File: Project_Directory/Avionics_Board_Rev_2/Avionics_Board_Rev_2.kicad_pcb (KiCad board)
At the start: 2 copper layers, 22 x 16 mm, 22 parts, among them J1 Battery, J10 PWM_1, J11 PWM_2, J12 PWM_3, J13 I2C, J14 UART, J2 ARM, J3 PYRO_1, J7 PWM_4, J8 PWM_5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

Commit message: more work
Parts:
- added C10: IRFR024NPBF, VelR:IRFR024NTRPBF-HXY Mosfet, F.Cu at (159.2, 154.5)
- added C7: IRFR024NPBF, VelR:IRFR024NTRPBF-HXY Mosfet, F.Cu at (161.5, 137.0)
- added C8: IRFR024NPBF, VelR:IRFR024NTRPBF-HXY Mosfet, F.Cu at (179.2, 168.9)
- added C9: IRFR024NPBF, VelR:IRFR024NTRPBF-HXY Mosfet, F.Cu at (179.2, 154.9)
- added D3: B120-E3, Diode_SMD:D_SMA, F.Cu at (186.6, 169.6)
- added D4: B120-E3, Diode_SMD:D_SMA, F.Cu at (187.0, 156.0)
- added D5: B120-E3, Diode_SMD:D_SMA, B.Cu at (153.8, 154.8)
- added J4: PYRO_1, TerminalBlock_Phoenix:TerminalBlock_Phoenix_MKDS-1,5-2_1x02_P5.00mm_Horizontal, F.Cu at (193.8, 171.3)
- added J5: PYRO_1, TerminalBlock_Phoenix:TerminalBlock_Phoenix_MKDS-1,5-2_1x02_P5.00mm_Horizontal, F.Cu at (193.8, 157.7)
- added J6: PYRO_1, TerminalBlock_Phoenix:TerminalBlock_Phoenix_MKDS-1,5-2_1x02_P5.00mm_Horizontal, F.Cu at (146.0, 152.3)
- added U2: LoRa, VelR:RFM95W, B.Cu at (188.4, 72.2)
- added U6: GPS, VelR:JST-SH 1mm 4 Pin Male E Type Vertical Single Row WTB Connector, F.Cu at (197.4, 73.4)
- J10, J11, J12, J7, J8, J9: footprint Connector_JST:JST_EH_B2B-EH-A_1x02_P2.50mm_Vertical -> Connector_PinHeader_2.54mm:PinHeader_1x03_P2.54mm_Vertical
- J3: footprint Connector_JST:JST_EH_B2B-EH-A_1x02_P2.50mm_Vertical -> TerminalBlock_Phoenix:TerminalBlock_Phoenix_MKDS-1,5-2_1x02_P5.00mm_Horizontal
- U10, U4, U5, U8: moved to B.Cu
- moved J13 140.6 mm to (197.0, 95.8), turned to 90 degrees
- moved J12 134.5 mm to (182.9, 114.4), turned to 90 degrees
- moved J11 134.1 mm to (182.8, 110.2), turned to 90 degrees
- moved J10 133.8 mm to (182.9, 106.4), turned to 90 degrees
- moved D1 120.7 mm to (153.4, 169.4), turned to 90 degrees
- moved J3 113.8 mm to (146.2, 166.7), turned to -90 degrees
- moved J2 109.2 mm to (195.2, 138.5), turned to 90 degrees
- moved U5 106.8 mm to (169.2, 149.4), turned to 90 degrees
- moved U4 101.0 mm to (182.2, 119.2), turned to 180 degrees
- moved C1 99.4 mm to (159.7, 169.6), turned to 90 degrees
- moved U10 93.4 mm to (155.0, 77.6), turned to 180 degrees
- moved J9 91.7 mm to (142.2, 114.2), turned to 90 degrees
- moved J8 91.4 mm to (142.1, 110.4), turned to 90 degrees
- moved J7 91.3 mm to (142.1, 106.2), turned to 90 degrees
- moved J14 90.2 mm to (143.0, 98.6), turned to 90 degrees
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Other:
- board size 22 x 16 mm -> 60 x 120 mm

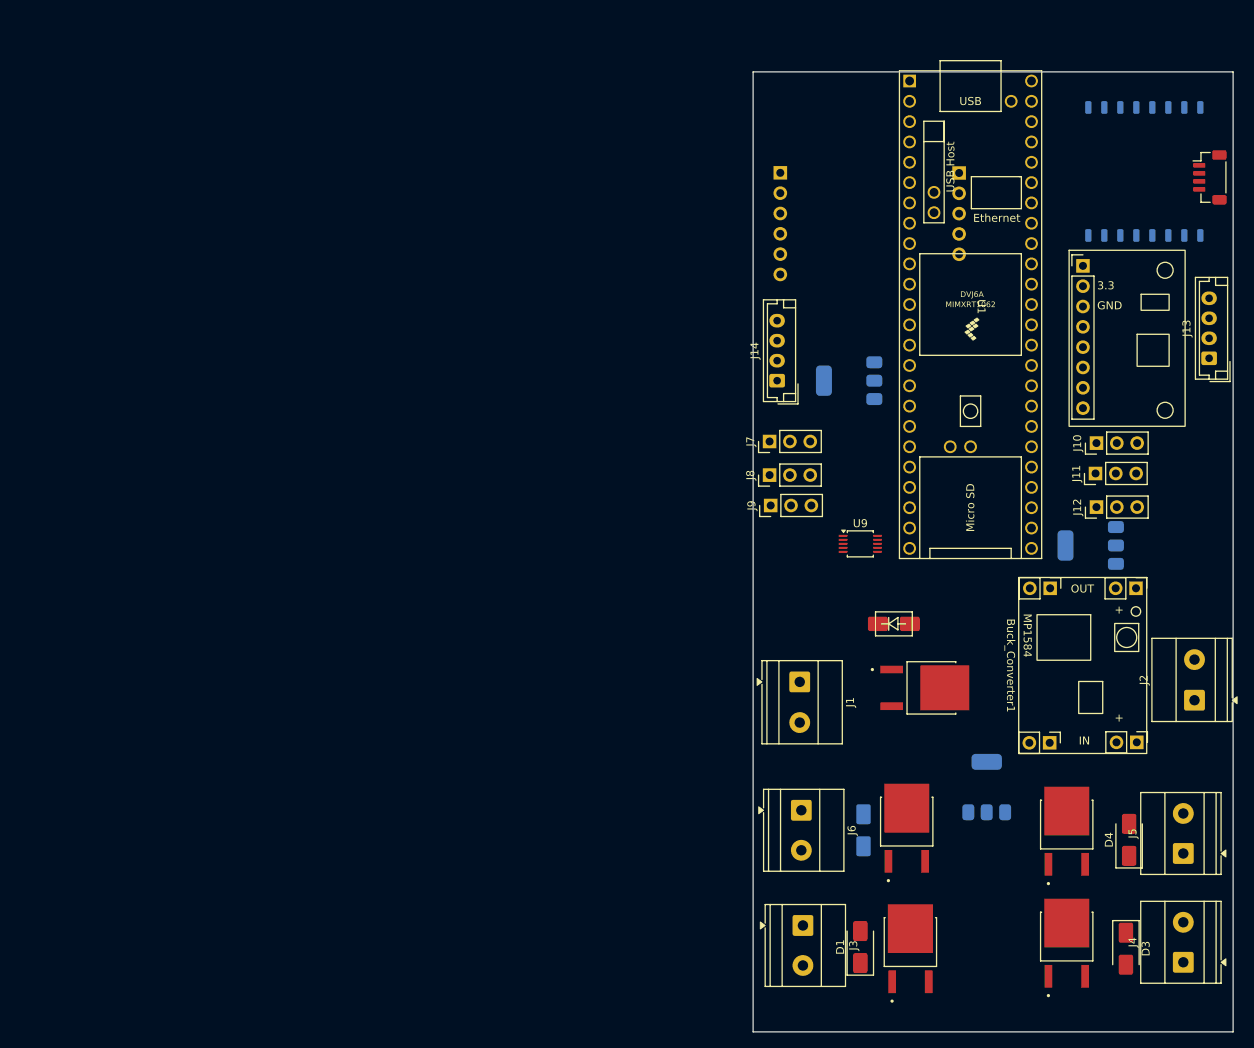
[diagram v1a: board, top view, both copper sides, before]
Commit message: modified gsm to be a jst connector
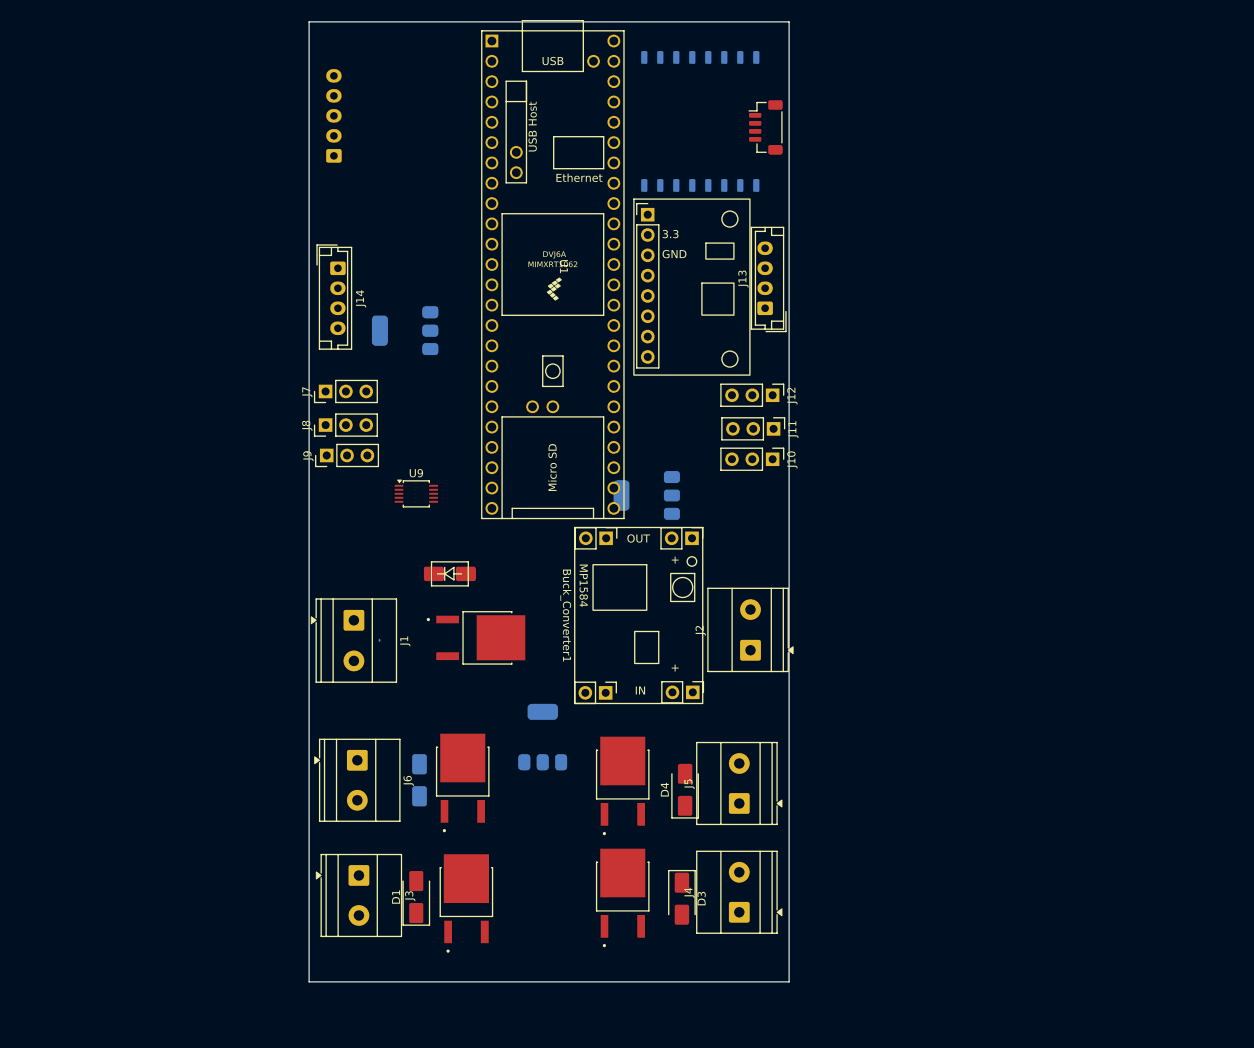
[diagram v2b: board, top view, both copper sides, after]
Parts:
- U10: footprint VelR:SIM800L -> Connector_JST:JST_EH_B5B-EH-A_1x05_P2.50mm_Vertical
- moved U10 67.8 mm to (87.6, 70.5), turned to 90 degrees
- moved J14 56.7 mm to (88.1, 84.5), turned to -90 degrees
- moved J1 56.3 mm to (90.1, 128.6)
- moved C7 55.9 mm to (106.0, 130.8)
- moved D5 55.9 mm to (98.3, 148.6)
- moved C1 55.9 mm to (104.2, 163.3)
- moved D1 55.9 mm to (97.9, 163.2)
- moved D2 55.9 mm to (102.1, 122.8)
- moved D3 55.9 mm to (131.1, 163.3)
- moved D4 55.9 mm to (131.5, 149.8)
- moved J13 55.9 mm to (141.5, 89.5)
- moved J2 55.9 mm to (139.7, 132.3)
- moved J4 55.9 mm to (138.3, 165.1)
- moved J5 55.9 mm to (138.3, 151.4)
- moved J6 55.9 mm to (90.5, 146.1)
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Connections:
- U10 pad 1: unconnected-(U10-NET-Pad1) -> (no net)

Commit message: changes to schematic
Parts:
- added C2: ~, Capacitor_SMD:C_0603_1608Metric_Pad1.08x0.95mm_HandSolder, F.Cu at (76.1, 61.7)
- added C3: ~, Capacitor_SMD:C_0603_1608Metric_Pad1.08x0.95mm_HandSolder, F.Cu at (76.1, 64.2)
- added C4: ~, Capacitor_SMD:C_0603_1608Metric_Pad1.08x0.95mm_HandSolder, F.Cu at (76.1, 66.7)
- added C5: ~, Capacitor_SMD:C_0603_1608Metric_Pad1.08x0.95mm_HandSolder, F.Cu at (76.1, 69.2)
- added C6: ~, Capacitor_SMD:C_0603_1608Metric_Pad1.08x0.95mm_HandSolder, F.Cu at (76.1, 71.8)
- added JP1: SolderJumper_3_Open, Jumper:SolderJumper-3_P2.0mm_Open_TrianglePad1.0x1.5mm, F.Cu at (99.2, 65.2)
- added R1: R, Resistor_SMD:R_1206_3216Metric_Pad1.30x1.75mm_HandSolder, F.Cu at (59.0, 62.1)
- added R10: R, Resistor_SMD:R_1206_3216Metric_Pad1.30x1.75mm_HandSolder, F.Cu at (65.0, 68.7)
- added R11: R, Resistor_SMD:R_1206_3216Metric_Pad1.30x1.75mm_HandSolder, F.Cu at (65.0, 72.0)
- added R12: R, Resistor_SMD:R_1206_3216Metric_Pad1.30x1.75mm_HandSolder, F.Cu at (65.0, 75.3)
- added R13: R, Resistor_SMD:R_1206_3216Metric_Pad1.30x1.75mm_HandSolder, F.Cu at (65.0, 78.7)
- added R14: R, Resistor_SMD:R_1206_3216Metric_Pad1.30x1.75mm_HandSolder, F.Cu at (65.0, 82.0)
- added R15: R, Resistor_SMD:R_1206_3216Metric_Pad1.30x1.75mm_HandSolder, F.Cu at (70.9, 62.1)
- added R16: R, Resistor_SMD:R_1206_3216Metric_Pad1.30x1.75mm_HandSolder, F.Cu at (70.9, 65.4)
- added R17: R, Resistor_SMD:R_1206_3216Metric_Pad1.30x1.75mm_HandSolder, F.Cu at (70.9, 68.7)
- added R18: R, Resistor_SMD:R_1206_3216Metric_Pad1.30x1.75mm_HandSolder, F.Cu at (70.9, 72.0)
- added R2: R, Resistor_SMD:R_1206_3216Metric_Pad1.30x1.75mm_HandSolder, F.Cu at (59.0, 65.4)
- added R3: R, Resistor_SMD:R_1206_3216Metric_Pad1.30x1.75mm_HandSolder, F.Cu at (59.0, 68.7)
- added R4: R, Resistor_SMD:R_1206_3216Metric_Pad1.30x1.75mm_HandSolder, F.Cu at (59.0, 72.0)
- added R5: R, Resistor_SMD:R_1206_3216Metric_Pad1.30x1.75mm_HandSolder, F.Cu at (59.0, 75.3)
- added R6: R, Resistor_SMD:R_1206_3216Metric_Pad1.30x1.75mm_HandSolder, F.Cu at (59.0, 78.7)
- added R7: R, Resistor_SMD:R_1206_3216Metric_Pad1.30x1.75mm_HandSolder, F.Cu at (59.0, 82.0)
- added R8: R, Resistor_SMD:R_1206_3216Metric_Pad1.30x1.75mm_HandSolder, F.Cu at (65.0, 62.1)
- added R9: R, Resistor_SMD:R_1206_3216Metric_Pad1.30x1.75mm_HandSolder, F.Cu at (65.0, 65.4)
- D1, D3, D4: moved to B.Cu
- U10: moved to F.Cu
- U2: value LoRa -> LoRa - RFM95-W/PW; footprint VelR:RFM95W -> VelR:RFM95W,PW
- moved U2 37.3 mm to (97.7, 78.5)
- moved U4 20.1 mm to (109.0, 122.4)
- moved J13 19.2 mm to (140.5, 70.4), turned to 180 degrees
- moved U8 9.84 mm to (101.2, 101.0)
- moved U6 7.57 mm to (141.4, 59.6)
- moved J2 7.48 mm to (139.0, 139.7)
- moved U10 6.71 mm to (87.2, 63.8), turned to -90 degrees
- moved J4 5.56 mm to (139.4, 170.5)
- moved J1 5.12 mm to (90.4, 133.7)
- moved J3 4.93 mm to (89.8, 165.3)
- moved U7 4.75 mm to (137.0, 84.6)
- moved U5 4.74 mm to (114.6, 147.8)
- moved D1 4.26 mm to (97.6, 167.4)
- moved J14 4.10 mm to (87.0, 80.6)
- moved U1 3.42 mm to (119.2, 84.6)
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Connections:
- U1 pad 17: unconnected-(U1-25_A11_RX6_SDA2-Pad17) -> /PWM_1
- U1 pad 20: unconnected-(U1-28_RX7-Pad20) -> /PWM_2
- U1 pad 21: unconnected-(U1-29_TX7-Pad21) -> /PWM_3
- U1 pad 25: unconnected-(U1-33_MCLK2-Pad25) -> /PWM_4
- U1 pad 28: unconnected-(U1-36_CS-Pad28) -> /PWM_5
- U1 pad 29: unconnected-(U1-37_CS-Pad29) -> /PWM_6
- U1 pad 4: unconnected-(U1-2_OUT2-Pad4) -> /LoRa_INT
- U1 pad 5: unconnected-(U1-3_LRCLK2-Pad5) -> /LoRa_DIO1
- U1 pad 6: unconnected-(U1-4_BCLK2-Pad6) -> /LoRa_CS
- U1 pad 7: unconnected-(U1-5_IN2-Pad7) -> /LoRa_RST
- U2 pad 1: unconnected-(U2-DIO2-Pad1) -> GND
- U2 pad 10: unconnected-(U2-MISO-Pad10) -> GND
- U2 pad 13: unconnected-(U2-NSS-Pad13) -> Net-(JP1-C)
- U2 pad 14: unconnected-(U2-RESET-Pad14) -> /LoRa_INT
- U2 pad 15: unconnected-(U2-DIO5-Pad15) -> /LoRa_DIO1
- U2 pad 2: unconnected-(U2-DIO1-Pad2) -> /SPI1_MISO
- U2 pad 3: unconnected-(U2-DIO0-Pad3) -> /SPI1_MOSI
- U2 pad 4: +3.3V -> /SPI1_SCK
- U2 pad 5: unconnected-(U2-DIO4-Pad5) -> /LoRa_CS
- U2 pad 6: unconnected-(U2-DIO3-Pad6) -> /LoRa_RST
- U2 pad 7: GND -> unconnected-(U2-DIO5-Pad7)
- U2 pad 8: unconnected-(U2-ANA-Pad8) -> GND
